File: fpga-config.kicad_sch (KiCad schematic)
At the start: 30 parts, among them J1 878321412, Q1 BSS138W-7-F, Q2 BSS138W-7-F, SW1 CVS-03B, U1 XC7K410T-2FFG900I, U2 TPD4E05U06QDQARQ1, U3 MAX1617AMEE+T

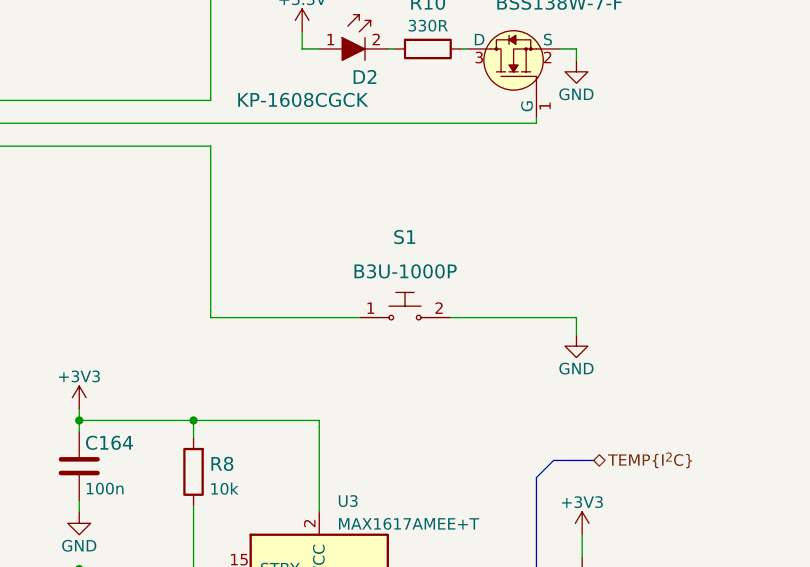
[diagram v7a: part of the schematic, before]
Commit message: Unify used buttons
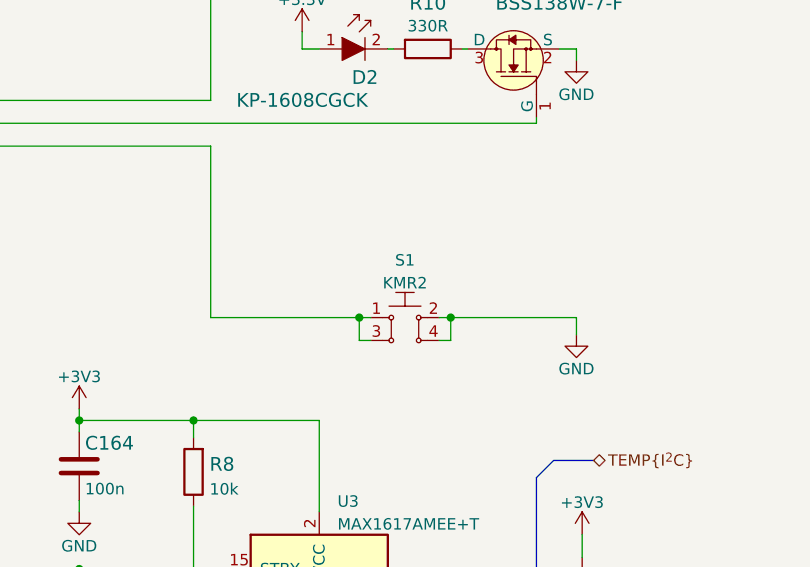
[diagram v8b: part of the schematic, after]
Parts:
- removed S1: B3U-1000P, antmicro-footprints:Switch_Tactile_SMD_B3U-1000P, symbol antmicroTactileSwitches:B3U-1000P
- added S1: KMR2, antmicro-footprints:SW_SPST_4.2x2.8, symbol antmicroPushbuttonSwitches:KMR2
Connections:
- net GND: now also S1.2, S1.4
- net PROGRAM_B: now also S1.1, S1.3
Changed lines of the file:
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@@
   (junction (at 38.1 227.33) (diameter 0) (color 0 0 0 0)
   )
+  (junction (at 330.835 152.4) (diameter 0) (color 0 0 0 0)
+  )
   (junction (at 190.5 135.89) (diameter 0) (color 0 0 0 0)
   )
@@
   )
   (junction (at 277.495 130.81) (diameter 0) (color 0 0 0 0)
+  )
+  (junction (at 340.995 152.4) (diameter 0) (color 0 0 0 0)
   )
   (junction (at 275.59 128.27) (diameter 0) (color 0 0 0 0)
@@
     (stroke (width 0) (type default) (color 0 0 0 0))
   )
+  (wire (pts (xy 330.835 152.4) (xy 332.105 152.4))
+    (stroke (width 0) (type default) (color 0 0 0 0))
+  )
   (wire (pts (xy 334.645 122.555) (xy 334.01 122.555))
     (stroke (width 0) (type default) (color 0 0 0 0))
@@
     (stroke (width 0) (type default) (color 0 0 0 0))
   )
+  (wire (pts (xy 340.995 154.94) (xy 340.995 152.4))
+    (stroke (width 0) (type default) (color 0 0 0 0))
+  )
   (wire (pts (xy 299.72 163.83) (xy 299.72 165.1))
     (stroke (width 0) (type default) (color 0 0 0 0))
@@
     (stroke (width 0) (type default) (color 0 0 0 0))
   )
-  (wire (pts (xy 340.995 152.4) (xy 354.965 152.4))
+  (wire (pts (xy 339.725 152.4) (xy 340.995 152.4))
     (stroke (width 0) (type default) (color 0 0 0 0))
   )
@@
   )
   (wire (pts (xy 350.52 130.81) (xy 350.52 130.175))
+    (stroke (width 0) (type default) (color 0 0 0 0))
+  )
+  (wire (pts (xy 330.835 152.4) (xy 330.835 154.94))
     (stroke (width 0) (type default) (color 0 0 0 0))
   )
@@
     (stroke (width 0) (type default) (color 0 0 0 0))
   )
+  (wire (pts (xy 330.835 154.94) (xy 332.105 154.94))
+    (stroke (width 0) (type default) (color 0 0 0 0))
+  )
   (wire (pts (xy 336.55 186.69) (xy 349.25 186.69))
     (stroke (width 0) (type default) (color 0 0 0 0))
@@
     (stroke (width 0) (type default) (color 0 0 0 0))
   )
+  (wire (pts (xy 340.995 152.4) (xy 354.965 152.4))
+    (stroke (width 0) (type default) (color 0 0 0 0))
+  )
   (wire (pts (xy 233.68 128.27) (xy 233.68 125.73))
     (stroke (width 0) (type default) (color 0 0 0 0))
@@
   )
   (wire (pts (xy 186.69 130.81) (xy 199.39 130.81))
+    (stroke (width 0) (type default) (color 0 0 0 0))
+  )
+  (wire (pts (xy 339.725 154.94) (xy 340.995 154.94))
     (stroke (width 0) (type default) (color 0 0 0 0))
   )
@@
     )
     (pin "1")
+  )
+  (symbol (lib_id "antmicroPushbuttonSwitches:KMR2") (at 335.915 152.4 0) (unit 1)
+    (in_bom yes) (on_board yes) (fields_autoplaced)
+    (property "Reference" "S1" (id 0) (at 335.915 146.0332 0))
+    (property "Value" "KMR2" (id 1) (at 335.915 148.5701 0))
+    (property "Footprint" "antmicro-footprints:SW_SPST_4.2x2.8" (id 2) (at 340.995 147.32 0)
+      (effects (font (size 1.27 1.27)) (justify left) hide)
+    )
+    (property "Datasheet" "http://www.farnell.com/datasheets/2631211.pdf" (id 3) (at 340.995 144.78 0)
+      (effects (font (size 1.524 1.524)) (justify left) hide)
+    )
+    (property "MPN" "KMR211NGLFS" (id 4) (at 340.8934 142.4178 0)
+      (effects (font (size 1.524 1.524)) (justify left) hide)
+    )
+    (property "Manufacturer" "C&K Components" (id 5) (at 340.995 140.4112 0)
+      (effects (font (size 1.524 1.524)) (justify left) hide)
+    )
+    (pin "1")
+    (pin "2")
+    (pin "3")
+    (pin "4")
   )
   (symbol (lib_id "antmicroSlideSwitches:CVS-03B") (at 90.805 133.35 0) (mirror y) (unit 1)
@@
     (pin "1")
   )
-  (symbol (lib_id "antmicroTactileSwitches:B3U-1000P") (at 335.915 152.4 0) (unit 1)
-    (in_bom yes) (on_board yes) (fields_autoplaced)
-    (property "Reference" "S1" (id 0) (at 335.915 143.51 0)
-      (effects (font (size 1.524 1.524)))
-    )
-    (property "Value" "B3U-1000P" (id 1) (at 335.915 147.32 0)
-      (effects (font (size 1.524 1.524)))
-    )
-    (property "Footprint" "antmicro-footprints:Switch_Tactile_SMD_B3U-1000P" (id 2) (at 340.995 147.32 0)
-      (effects (font (size 1.524 1.524)) (justify left) hide)
-    )
-    (property "Datasheet" "https://omronfs.omron.com/en_US/ecb/products/pdf/en-b3u.pdf" (id 3) (at 340.995 144.78 0)
-      (effects (font (size 1.524 1.524)) (justify left) hide)
-    )
-    (property "MPN" "B3U-1000P" (id 4) (at 340.995 139.7 0)
-      (effects (font (size 1.524 1.524)) (justify left) hide)
-    )
-    (property "Manufacturer" "Omron Electronics Inc-EMC Div" (id 5) (at 340.995 124.46 0)
-      (effects (font (size 1.524 1.524)) (justify left) hide)
-    )
-    (pin "1")
-    (pin "2")
-  )
   (symbol (lib_id "antmicroTVSDiodes:TPD4E05U06QDQARQ1") (at 66.04 245.745 270) (unit 1)
